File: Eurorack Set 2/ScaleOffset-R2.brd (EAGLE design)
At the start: 29.1 x 106.5 mm, 32 parts, among them IC3 TL074D

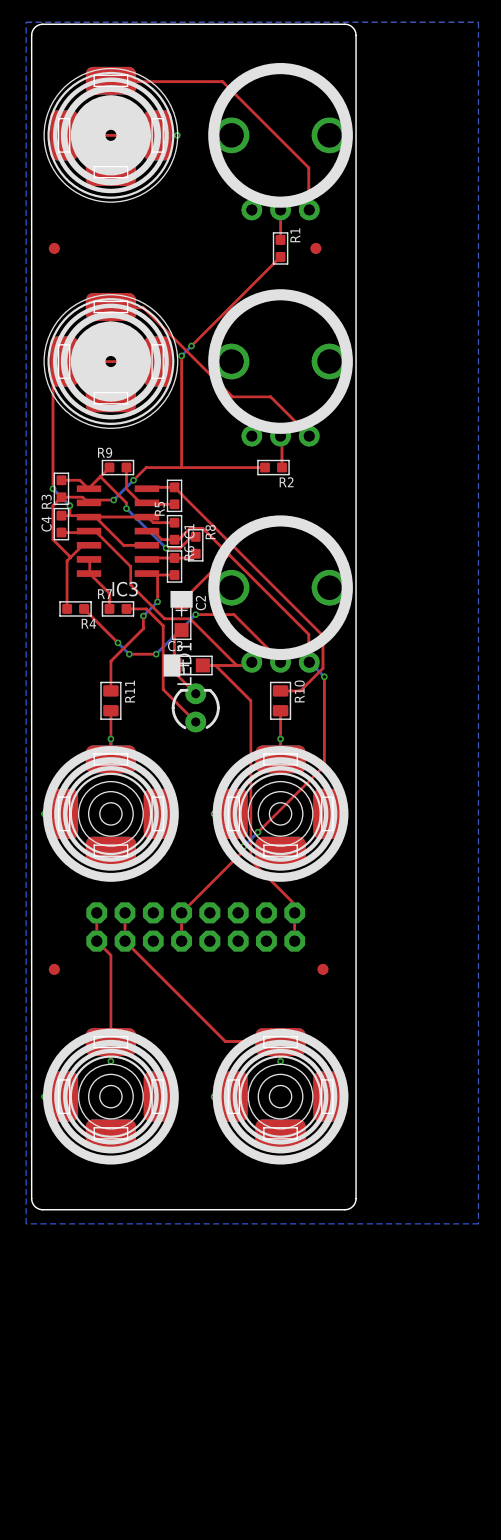
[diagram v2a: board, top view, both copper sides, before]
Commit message: Updated library shape for jacks - updated all boards to match
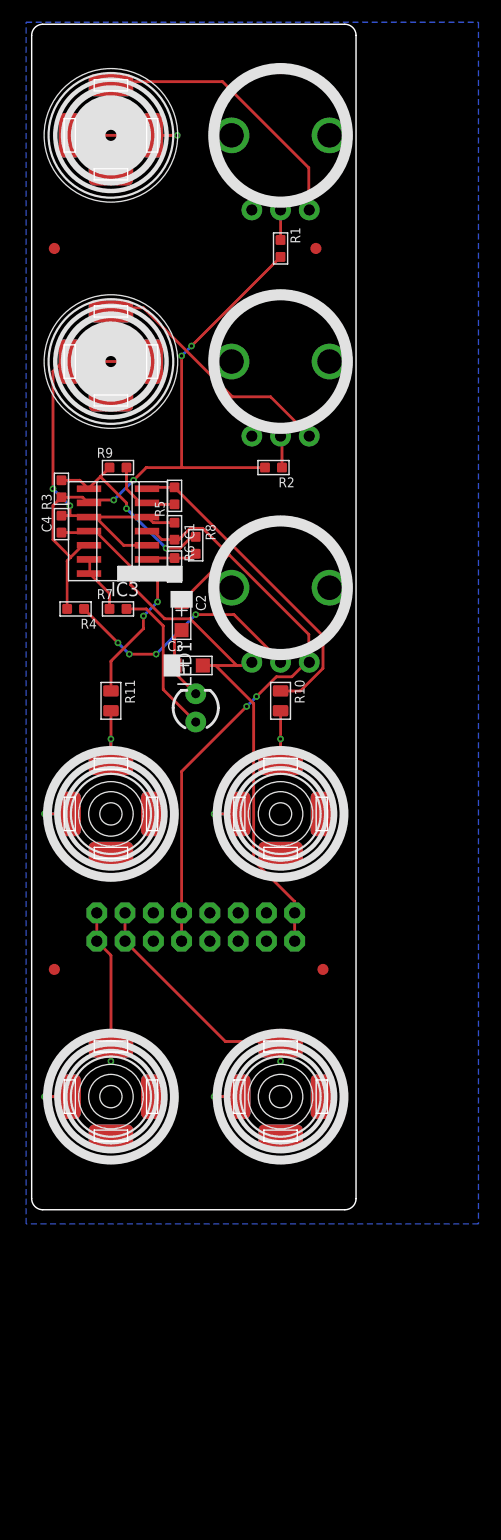
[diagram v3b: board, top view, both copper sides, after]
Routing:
- net GND: track 74.7 -> 77.7 mm
- net OUT2: track 6.20 -> 7.00 mm
- net OUT1: track 6.20 -> 7.00 mm
- net 12V: track 58.7 -> 58.6 mm, vias 3 -> 2
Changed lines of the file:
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@@
 <wire x1="10.922" y1="62.23" x2="11.43" y2="61.722" width="0.254" layer="1"/>
 <wire x1="10.922" y1="62.23" x2="10.855" y2="62.23" width="0.254" layer="1"/>
-<wire x1="11.82" y1="76.2" x2="10.033" y2="76.2" width="0.254" layer="1"/>
-<wire x1="10.033" y1="76.2" x2="3.42" y2="76.2" width="0.254" layer="1"/>
-<wire x1="1.651" y1="10.16" x2="3.42" y2="10.16" width="0.254" layer="1"/>
-<wire x1="3.42" y1="10.16" x2="1.651" y2="10.16" width="0.254" layer="16"/>
-<wire x1="13.589" y1="96.52" x2="11.82" y2="96.52" width="0.254" layer="16"/>
-<wire x1="11.82" y1="96.52" x2="13.589" y2="96.52" width="0.254" layer="1"/>
-<wire x1="16.891" y1="10.16" x2="18.66" y2="10.16" width="0.254" layer="1"/>
-<wire x1="18.66" y1="10.16" x2="16.891" y2="10.16" width="0.254" layer="16"/>
-<wire x1="1.651" y1="35.56" x2="3.42" y2="35.56" width="0.254" layer="1"/>
-<wire x1="3.42" y1="35.56" x2="1.651" y2="35.56" width="0.254" layer="16"/>
-<wire x1="11.82" y1="96.52" x2="3.42" y2="96.52" width="0.254" layer="1"/>
-<wire x1="16.891" y1="35.56" x2="18.66" y2="35.56" width="0.254" layer="1"/>
-<wire x1="18.66" y1="35.56" x2="16.891" y2="35.56" width="0.254" layer="16"/>
-<wire x1="11.82" y1="76.2" x2="10.033" y2="76.2" width="0.254" layer="16"/>
+<wire x1="11.32" y1="76.2" x2="10.033" y2="76.2" width="0.254" layer="1"/>
+<wire x1="10.033" y1="76.2" x2="3.92" y2="76.2" width="0.254" layer="1"/>
+<wire x1="1.651" y1="10.16" x2="3.92" y2="10.16" width="0.254" layer="1"/>
+<wire x1="3.92" y1="10.16" x2="1.651" y2="10.16" width="0.254" layer="16"/>
+<wire x1="13.589" y1="96.52" x2="11.32" y2="96.52" width="0.254" layer="16"/>
+<wire x1="11.32" y1="96.52" x2="13.589" y2="96.52" width="0.254" layer="1"/>
+<wire x1="16.891" y1="10.16" x2="19.16" y2="10.16" width="0.254" layer="1"/>
+<wire x1="19.16" y1="10.16" x2="16.891" y2="10.16" width="0.254" layer="16"/>
+<wire x1="1.651" y1="35.56" x2="3.92" y2="35.56" width="0.254" layer="1"/>
+<wire x1="3.92" y1="35.56" x2="1.651" y2="35.56" width="0.254" layer="16"/>
+<wire x1="11.32" y1="96.52" x2="3.92" y2="96.52" width="0.254" layer="1"/>
+<wire x1="16.891" y1="35.56" x2="19.16" y2="35.56" width="0.254" layer="1"/>
+<wire x1="19.16" y1="35.56" x2="16.891" y2="35.56" width="0.254" layer="16"/>
+<wire x1="11.32" y1="76.2" x2="10.033" y2="76.2" width="0.254" layer="16"/>
 <wire x1="3.937" y1="63.246" x2="3.937" y2="62.357" width="0.254" layer="1"/>
 <wire x1="2.413" y1="64.77" x2="3.937" y2="63.246" width="0.254" layer="16"/>
 <wire x1="2.413" y1="75.311" x2="2.413" y2="64.77" width="0.254" layer="1"/>
 <wire x1="3.302" y1="76.2" x2="2.413" y2="75.311" width="0.254" layer="1"/>
-<wire x1="3.302" y1="76.2" x2="3.42" y2="76.2" width="0.254" layer="1"/>
+<wire x1="3.302" y1="76.2" x2="3.92" y2="76.2" width="0.254" layer="1"/>
 <via x="1.651" y="10.16" extent="1-16" drill="0.3048"/>
 <via x="13.589" y="96.52" extent="1-16" drill="0.3048"/>
@@
 <contactref element="C2" pad="+"/>
 <wire x1="18.2245" y1="58.8645" x2="13.97" y2="54.61" width="0.254" layer="1"/>
-<wire x1="26.797" y1="47.879" x2="25.527" y2="49.149" width="0.254" layer="16"/>
-<wire x1="26.797" y1="39.878" x2="26.797" y2="47.879" width="0.254" layer="1"/>
-<wire x1="20.828" y1="33.909" x2="26.797" y2="39.878" width="0.254" layer="1"/>
-<wire x1="19.558" y1="32.639" x2="20.828" y2="33.909" width="0.254" layer="16"/>
-<wire x1="19.558" y1="32.258" x2="19.558" y2="32.639" width="0.254" layer="1"/>
-<wire x1="13.97" y1="26.67" x2="19.558" y2="32.258" width="0.254" layer="1"/>
-<wire x1="25.527" y1="49.149" x2="25.44" y2="49.18" width="0.254" layer="16"/>
-<via x="26.797" y="47.879" extent="1-16" drill="0.3048"/>
-<via x="20.828" y="33.909" extent="1-16" drill="0.3048"/>
-<via x="19.558" y="32.639" extent="1-16" drill="0.3048"/>
+<wire x1="13.97" y1="39.37" x2="13.97" y2="26.67" width="0.254" layer="1"/>
+<wire x1="19.812" y1="45.212" x2="13.97" y2="39.37" width="0.254" layer="1"/>
+<wire x1="20.701" y1="46.101" x2="19.812" y2="45.212" width="0.254" layer="16"/>
+<wire x1="22.479" y1="47.879" x2="20.701" y2="46.101" width="0.254" layer="1"/>
+<wire x1="23.876" y1="47.879" x2="22.479" y2="47.879" width="0.254" layer="1"/>
+<wire x1="25.273" y1="49.276" x2="23.876" y2="47.879" width="0.254" layer="1"/>
+<wire x1="25.273" y1="49.276" x2="25.44" y2="49.18" width="0.254" layer="1"/>
+<via x="19.812" y="45.212" extent="1-16" drill="0.3048"/>
+<via x="20.701" y="46.101" extent="1-16" drill="0.3048"/>
 </signal>
 <signal name="-12V">
@@
 <wire x1="14.732" y1="53.086" x2="12.446" y2="53.086" width="0.254" layer="1"/>
 <wire x1="18.923" y1="48.895" x2="14.732" y2="53.086" width="0.254" layer="1"/>
-<wire x1="24.13" y1="27.432" x2="24.13" y2="26.67" width="0.254" layer="1"/>
-<wire x1="20.193" y1="31.369" x2="24.13" y2="27.432" width="0.254" layer="1"/>
-<wire x1="20.193" y1="45.72" x2="20.193" y2="31.369" width="0.254" layer="1"/>
-<wire x1="17.018" y1="48.895" x2="20.193" y2="45.72" width="0.254" layer="1"/>
+<wire x1="24.13" y1="27.686" x2="24.13" y2="26.67" width="0.254" layer="1"/>
+<wire x1="20.447" y1="31.369" x2="24.13" y2="27.686" width="0.254" layer="1"/>
+<wire x1="20.447" y1="45.466" x2="20.447" y2="31.369" width="0.254" layer="1"/>
+<wire x1="17.018" y1="48.895" x2="20.447" y2="45.466" width="0.254" layer="1"/>
 </signal>
 <signal name="OFFSET">
@@
 <wire x1="7.62" y1="81.026" x2="10.541" y2="81.026" width="0.254" layer="1"/>
 <wire x1="25.4" y1="69.596" x2="25.44" y2="69.5" width="0.254" layer="1"/>
-<wire x1="7.62" y1="79.375" x2="7.62" y2="81.1" width="0.254" layer="16"/>
-<wire x1="7.62" y1="81.026" x2="7.62" y2="79.375" width="0.254" layer="1"/>
-<wire x1="7.62" y1="81.026" x2="7.62" y2="81.1" width="0.254" layer="1"/>
+<wire x1="7.62" y1="79.375" x2="7.62" y2="80.7" width="0.254" layer="16"/>
+<wire x1="7.62" y1="80.7" x2="7.62" y2="79.375" width="0.254" layer="1"/>
+<wire x1="7.62" y1="81.026" x2="7.62" y2="80.7" width="0.254" layer="1"/>
 <via x="7.62" y="79.375" extent="1-16" drill="0.3048"/>
 </signal>
@@
 <wire x1="7.62" y1="101.346" x2="17.653" y2="101.346" width="0.254" layer="1"/>
 <wire x1="25.4" y1="89.916" x2="25.44" y2="89.82" width="0.254" layer="1"/>
-<wire x1="7.62" y1="99.695" x2="7.62" y2="101.42" width="0.254" layer="16"/>
-<wire x1="7.62" y1="101.346" x2="7.62" y2="99.695" width="0.254" layer="1"/>
-<wire x1="7.62" y1="101.346" x2="7.62" y2="101.42" width="0.254" layer="1"/>
+<wire x1="7.62" y1="99.695" x2="7.62" y2="101.02" width="0.254" layer="16"/>
+<wire x1="7.62" y1="101.02" x2="7.62" y2="99.695" width="0.254" layer="1"/>
+<wire x1="7.62" y1="101.346" x2="7.62" y2="101.02" width="0.254" layer="1"/>
 <via x="7.62" y="99.695" extent="1-16" drill="0.3048"/>
 </signal>
@@
 <contactref element="CV" pad="TIP@2"/>
 <contactref element="CV" pad="TIP@1"/>
-<wire x1="22.86" y1="13.335" x2="22.86" y2="15.06" width="0.254" layer="16"/>
-<wire x1="22.86" y1="15.06" x2="22.86" y2="13.335" width="0.254" layer="1"/>
+<wire x1="22.86" y1="13.335" x2="22.86" y2="14.66" width="0.254" layer="16"/>
+<wire x1="22.86" y1="14.66" x2="22.86" y2="13.335" width="0.254" layer="1"/>
 <wire x1="8.89" y1="26.67" x2="8.89" y2="24.13" width="0.254" layer="1"/>
 <wire x1="17.907" y1="15.113" x2="22.86" y2="15.113" width="0.254" layer="1"/>
 <wire x1="8.89" y1="24.13" x2="17.907" y2="15.113" width="0.254" layer="1"/>
-<wire x1="22.86" y1="15.113" x2="22.86" y2="15.06" width="0.254" layer="1"/>
+<wire x1="22.86" y1="15.113" x2="22.86" y2="14.66" width="0.254" layer="1"/>
 <via x="22.86" y="13.335" extent="1-16" drill="0.3048"/>
 </signal>
@@
 <contactref element="GATE" pad="TIP@2"/>
 <contactref element="GATE" pad="TIP@1"/>
-<wire x1="7.62" y1="13.335" x2="7.62" y2="15.06" width="0.254" layer="16"/>
-<wire x1="7.62" y1="15.06" x2="7.62" y2="13.335" width="0.254" layer="1"/>
+<wire x1="7.62" y1="13.335" x2="7.62" y2="14.66" width="0.254" layer="16"/>
+<wire x1="7.62" y1="14.66" x2="7.62" y2="13.335" width="0.254" layer="1"/>
 <wire x1="6.35" y1="26.67" x2="6.35" y2="24.13" width="0.254" layer="1"/>
-<wire x1="7.62" y1="22.86" x2="7.62" y2="15.06" width="0.254" layer="1"/>
+<wire x1="7.62" y1="22.86" x2="7.62" y2="14.66" width="0.254" layer="1"/>
 <wire x1="6.35" y1="24.13" x2="7.62" y2="22.86" width="0.254" layer="1"/>
 <via x="7.62" y="13.335" extent="1-16" drill="0.3048"/>
@@
 <contactref element="OUT1" pad="TIP@2"/>
 <contactref element="R10" pad="2"/>
-<wire x1="22.86" y1="40.46" x2="22.86" y2="42.291" width="0.254" layer="1"/>
+<wire x1="22.86" y1="40.06" x2="22.86" y2="42.291" width="0.254" layer="1"/>
 <wire x1="22.86" y1="42.291" x2="22.86" y2="44.831" width="0.254" layer="1"/>
-<wire x1="22.86" y1="42.291" x2="22.86" y2="40.46" width="0.254" layer="16"/>
+<wire x1="22.86" y1="42.291" x2="22.86" y2="40.06" width="0.254" layer="16"/>
 <via x="22.86" y="42.291" extent="1-16" drill="0.3048"/>
 </signal>
@@
 <contactref element="OUT2" pad="TIP@2"/>
 <contactref element="R11" pad="2"/>
-<wire x1="7.62" y1="40.46" x2="7.62" y2="42.291" width="0.254" layer="1"/>
+<wire x1="7.62" y1="40.06" x2="7.62" y2="42.291" width="0.254" layer="1"/>
 <wire x1="7.62" y1="42.291" x2="7.62" y2="44.831" width="0.254" layer="1"/>
-<wire x1="7.62" y1="42.291" x2="7.62" y2="40.46" width="0.254" layer="16"/>
+<wire x1="7.62" y1="42.291" x2="7.62" y2="40.06" width="0.254" layer="16"/>
 <via x="7.62" y="42.291" extent="1-16" drill="0.3048"/>
 </signal>
